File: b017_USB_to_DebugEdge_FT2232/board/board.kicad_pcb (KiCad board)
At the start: 4 copper layers, 21 x 29 mm, 31 parts, among them J1 008_USB_2x2, J2 DebugEdge_02x05, U1 93CxxC, U2 FT2232H, Y1 Crystal_GND24

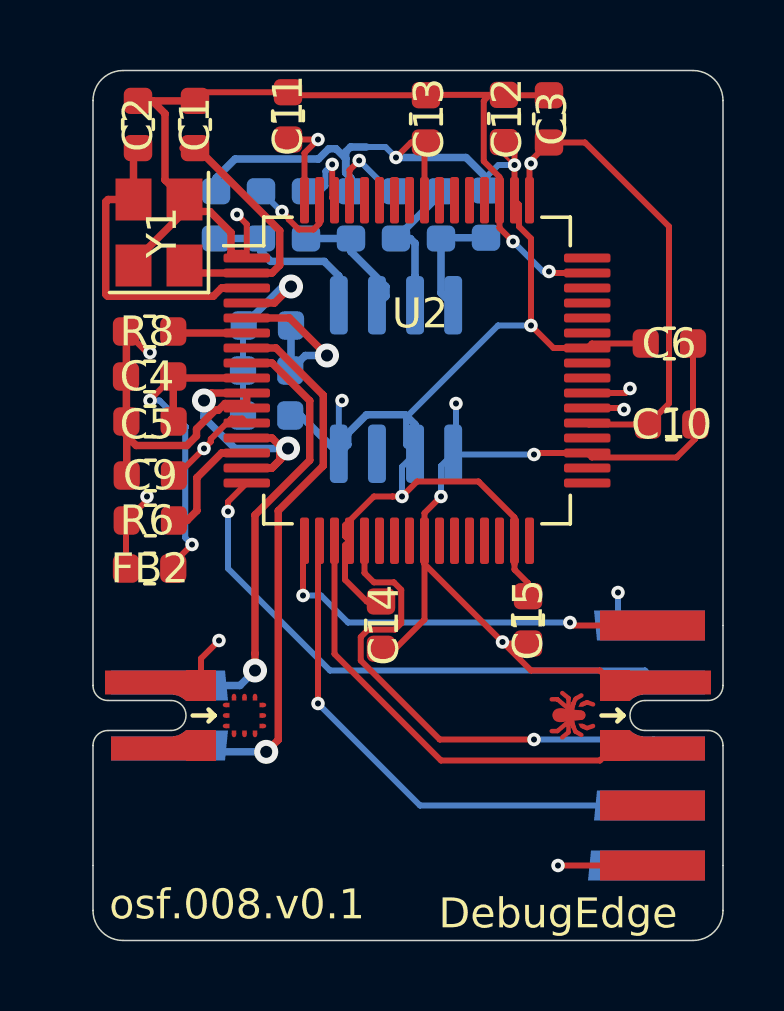
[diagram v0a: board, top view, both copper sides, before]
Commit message: modernized to kicad 6 and added missing LDO
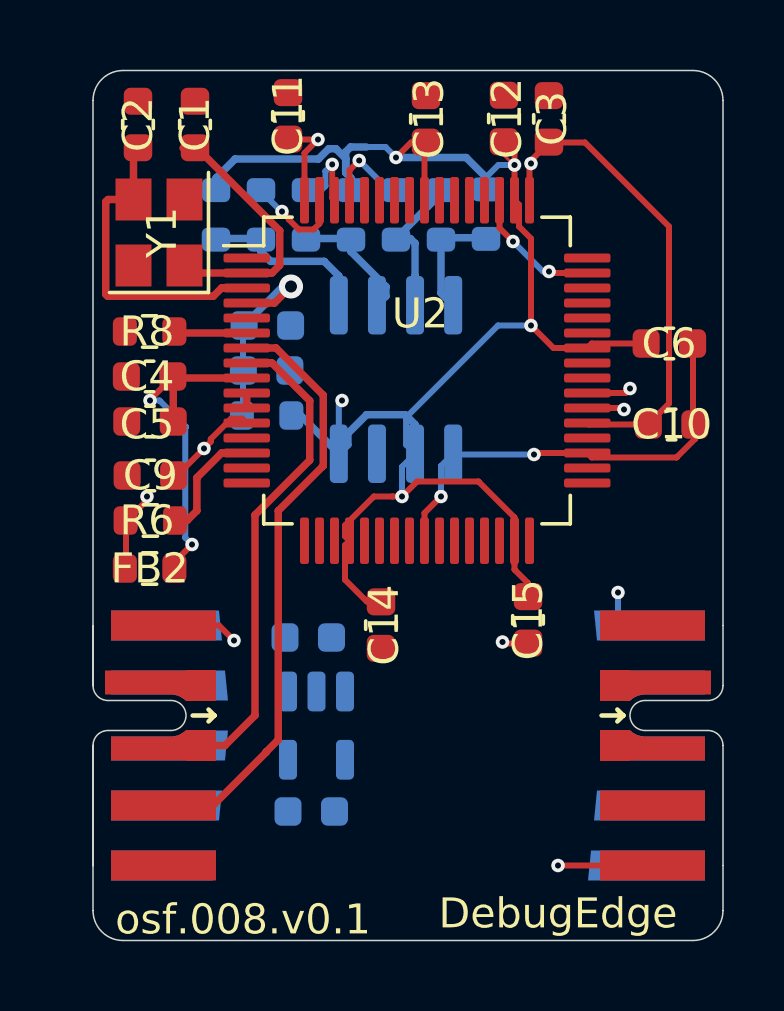
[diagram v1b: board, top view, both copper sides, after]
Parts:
- added C16: 100nF, Capacitor_SMD:C_0603_1608Metric, B.Cu at (137.2, 102.9)
- added C17: 100nF, Capacitor_SMD:C_0603_1608Metric, B.Cu at (137.3, 108.7)
- added U3: TC1017-xCT, Package_TO_SOT_SMD:SOT-23-5, B.Cu at (137.4, 105.8)
- J1: footprint on_edge:on_edge_2x02_device -> on_edge:on_edge_2x05_device
- Y1: value Crystal_GND24 -> 12MHz
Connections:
- net /Sheet603703E3/~reset renamed /Sheet603703E3/~{reset}
- J2 pad 10: (no net) -> unconnected-(J2-Pad10)
- J2 pad 5: (no net) -> /Sheet603703E3/Vref
- U1 pad 7: (no net) -> unconnected-(U1-Pad7)
- U2 pad 22: (no net) -> unconnected-(U2-Pad22)
- U2 pad 23: (no net) -> unconnected-(U2-Pad23)
- U2 pad 24: (no net) -> unconnected-(U2-Pad24)
- U2 pad 26: (no net) -> unconnected-(U2-Pad26)
- U2 pad 27: (no net) -> unconnected-(U2-Pad27)
- U2 pad 28: (no net) -> unconnected-(U2-Pad28)
- U2 pad 29: (no net) -> unconnected-(U2-Pad29)
- U2 pad 30: (no net) -> unconnected-(U2-Pad30)
- U2 pad 32: (no net) -> unconnected-(U2-Pad32)
- U2 pad 33: (no net) -> unconnected-(U2-Pad33)
- U2 pad 34: (no net) -> unconnected-(U2-Pad34)
- U2 pad 36: (no net) -> unconnected-(U2-Pad36)
- U2 pad 40: (no net) -> unconnected-(U2-Pad40)
- U2 pad 41: (no net) -> unconnected-(U2-Pad41)
- U2 pad 43: (no net) -> unconnected-(U2-Pad43)
- U2 pad 44: (no net) -> unconnected-(U2-Pad44)
- U2 pad 45: (no net) -> unconnected-(U2-Pad45)
- U2 pad 46: (no net) -> unconnected-(U2-Pad46)
- U2 pad 48: (no net) -> unconnected-(U2-Pad48)
- U2 pad 52: (no net) -> unconnected-(U2-Pad52)
- U2 pad 53: (no net) -> unconnected-(U2-Pad53)
- U2 pad 54: (no net) -> unconnected-(U2-Pad54)
- U2 pad 55: (no net) -> unconnected-(U2-Pad55)
- U2 pad 57: (no net) -> unconnected-(U2-Pad57)
- U2 pad 58: (no net) -> unconnected-(U2-Pad58)
- U2 pad 59: (no net) -> unconnected-(U2-Pad59)
- U2 pad 60: (no net) -> unconnected-(U2-Pad60)
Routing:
- net GND: track 125.4 -> 32.3 mm, vias 12 -> 6
- net /Sheet603703E3/TCK: track 19.1 -> 0.00 mm, vias 1 -> 0
- net /Sheet603703E3/TDO: track 18.0 -> 0.00 mm, vias 1 -> 0
- net /Sheet603703E3/~{reset}: track 17.1 -> 0.00 mm, vias 1 -> 0
- net /Sheet603703E3/TMS: track 14.8 -> 0.00 mm
- net /Sheet603703E3/TDI: track 13.9 -> 0.00 mm, vias 2 -> 0
- net /Sheet603703E3/DP: track 17.5 -> 16.1 mm, vias 1 -> 0
- net /Sheet603703E3/DM: track 19.6 -> 20.1 mm, vias 1 -> 0
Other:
- net class Default removed

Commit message: reorganized components so that silk screen has room
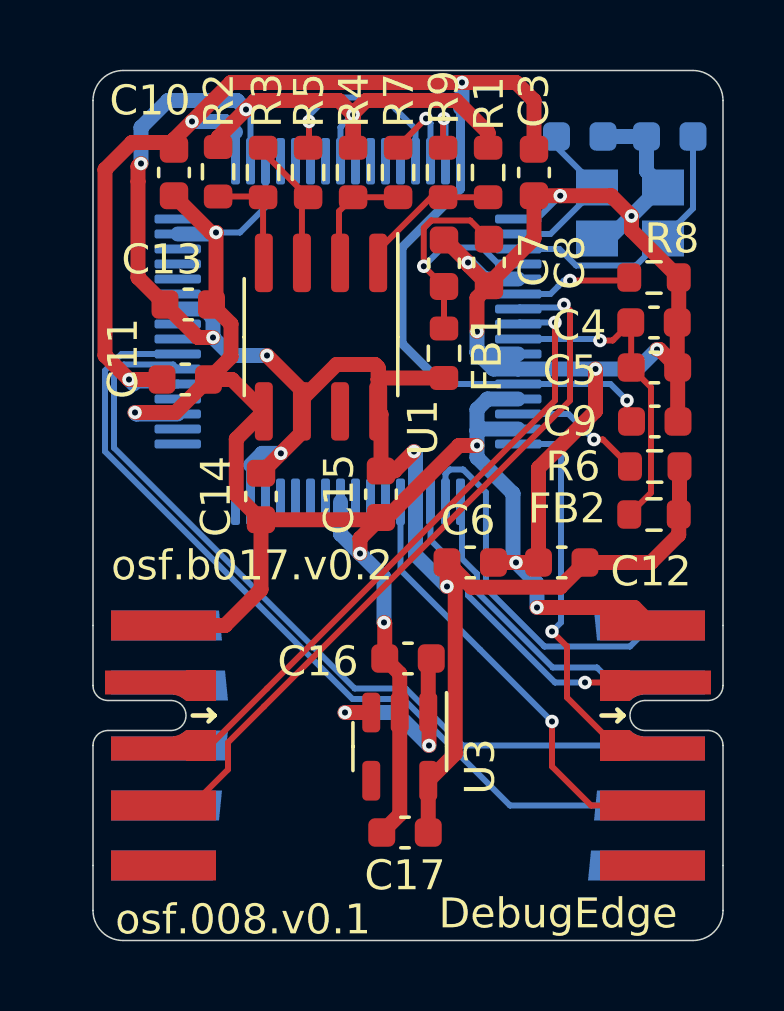
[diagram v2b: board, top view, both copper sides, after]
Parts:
- C1, C2, U2, Y1: moved to B.Cu
- C16, C17, C7, C8, FB1, R1, R2, R3, R4, R5, R7, R9, U1, U3: moved to F.Cu
- moved C10 18.6 mm to (132.7, 87.4), turned to -90 degrees
- moved C2 17.7 mm to (149.2, 86.2), turned to 180 degrees
- moved C4 16.9 mm to (148.7, 92.4), turned to 0 degrees
- moved C5 16.9 mm to (148.7, 93.9), turned to 0 degrees
- moved C9 16.9 mm to (148.7, 95.7), turned to 0 degrees
- moved FB2 16.9 mm to (148.7, 98.8), turned to 0 degrees
- moved R6 16.9 mm to (148.7, 97.2), turned to 0 degrees
- moved R8 16.9 mm to (148.7, 90.9), turned to 0 degrees
- moved Y1 15.7 mm to (147.9, 88.8), turned to 0 degrees
- moved C12 14.9 mm to (145.6, 100.4), turned to 180 degrees
- moved C1 12.8 mm to (146.2, 86.2), turned to 0 degrees
- moved C13 10.1 mm to (133.2, 91.8), turned to 0 degrees
- moved C6 9.87 mm to (142.6, 100.4)
- moved C11 9.43 mm to (133.1, 94.3), turned to 0 degrees
- moved R1 9.18 mm to (143.2, 87.4)
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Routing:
- net GND: track 32.3 -> 112.3 mm, vias 6 -> 13
- net /Sheet603703E3/TX: track 9.57 -> 27.1 mm, vias 2 -> 0
- net /Sheet603703E3/~{reset}: track 0.00 -> 14.8 mm, vias 0 -> 1
- net /Sheet603703E3/TDO: track 0.00 -> 12.4 mm
- net /Sheet603703E3/TCK: track 0.00 -> 12.4 mm, vias 0 -> 1
- net /Sheet603703E3/TDI: track 0.00 -> 10.6 mm
- net /Sheet603703E3/TMS: track 0.00 -> 9.79 mm, vias 0 -> 1
- net +3V3: track 68.9 -> 77.5 mm, vias 6 -> 8
- net /Sheet603703E3/VCC: track 0.00 -> 7.08 mm, vias 0 -> 2
- net /Sheet603703E3/RX: track 23.8 -> 28.4 mm, vias 2 -> 0
- net /Sheet603703E3/DM: track 20.1 -> 24.5 mm, vias 0 -> 1
- net /Sheet603703E3/DP: track 16.1 -> 20.4 mm, vias 0 -> 1
- net +1V8: track 45.1 -> 49.1 mm, vias 3 -> 4
- net Net-(C1-Pad1): track 8.90 -> 5.53 mm
- net Net-(R5-Pad1): track 3.11 -> 6.40 mm
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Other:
- outline, holes or cut-outs redrawn
- board text added: "osf.b017.v0.2"
